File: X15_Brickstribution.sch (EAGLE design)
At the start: 85 parts, among them Q1 310mA/60V/1.6Ω, U5 IC_L4970A, U6 DIODE_STPS1545CT, U7 IC_L4970A, U8 DIODE_STPS1545CT

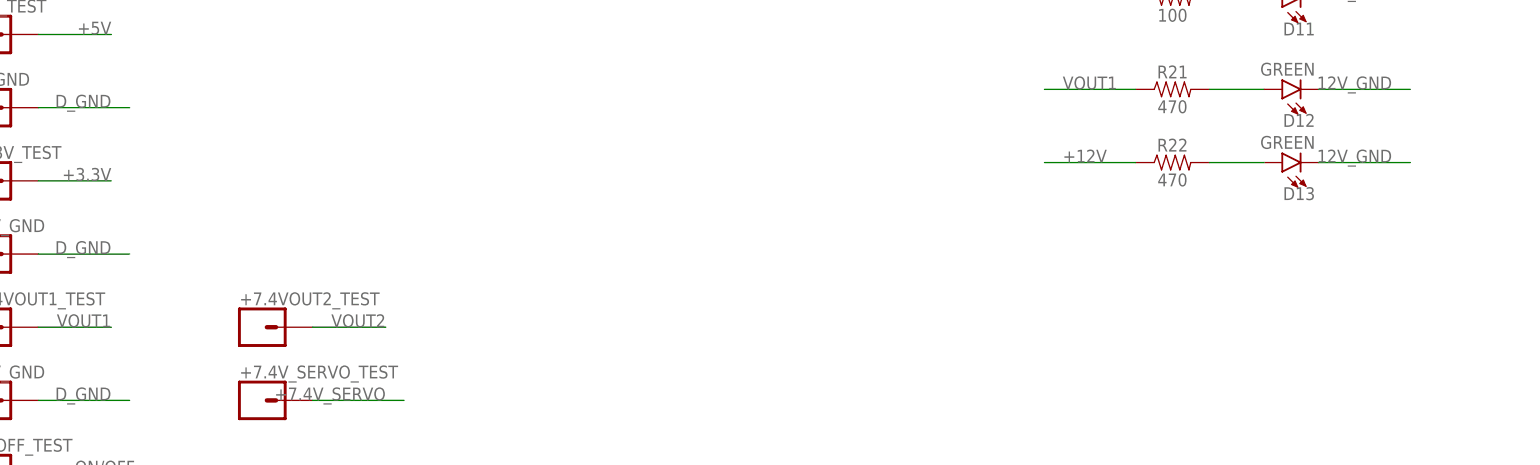
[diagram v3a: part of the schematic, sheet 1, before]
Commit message: Revision V3 Schematic - LED's added for current source
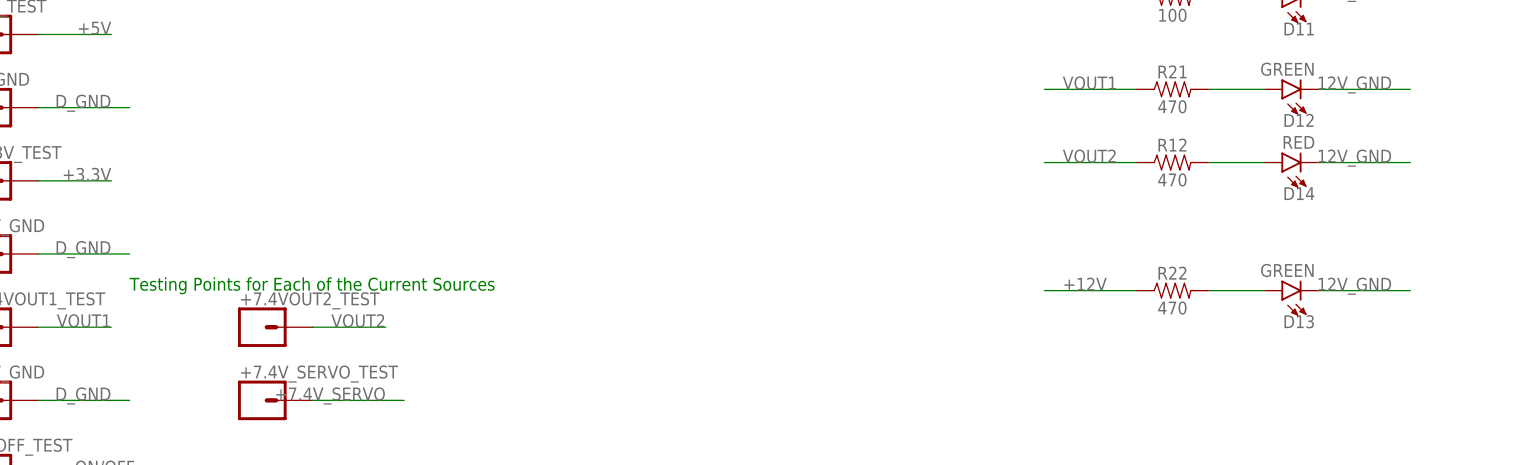
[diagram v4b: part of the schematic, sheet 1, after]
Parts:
- added D14: RED, SparkFun-LED:LED-RED0603
- added R12: 470, SparkFun-Resistors:470OHM-0603-1/10W-1%
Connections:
- new net N$11: D14.A, R12.2
- net 12V_GND: now also D14.C
- net VOUT2: now also R12.1
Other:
- note added: "Testing Points for Each of the Current Sources"
- moved on the sheet: D13, R22
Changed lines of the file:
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@@
 <part name="BACKPLANE_POWER" library="X15_Brickstribution" deviceset="CONN_MPPT-10-01-01-L-RA-SD" device=""/>
 <part name="U$2" library="X15_Brickstribution" deviceset="CONN_BMR480_CONNECTOR" device=""/>
+<part name="R12" library="SparkFun-Resistors" library_urn="urn:adsk.eagle:library:532" deviceset="470OHM" device="-0603-1/10W-1%" package3d_urn="urn:adsk.eagle:package:39650/1" value="470"/>
+<part name="D14" library="SparkFun-LED" library_urn="urn:adsk.eagle:library:529" deviceset="LED-RED" device="0603" package3d_urn="urn:adsk.eagle:package:39354/1" value="RED"/>
 </parts>
 <sheets>
@@
 <text x="227.838" y="124.206" size="1.4224" layer="91">Latch that keeps ON/OFF low after it first goes low</text>
 <text x="317.754" y="125.73" size="2.1844" layer="91">LED Testing</text>
+<text x="170.18" y="35.56" size="1.778" layer="91">Testing Points for Each of the Current Sources</text>
 </plain>
 <instances>
@@
 <attribute name="VALUE" x="334.772" y="65.405" size="1.778" layer="96" font="vector" rot="R180" align="top-left"/>
 </instance>
-<instance part="R22" gate="G$1" x="314.96" y="53.34" smashed="yes">
-<attribute name="NAME" x="314.96" y="54.864" size="1.778" layer="95" font="vector" align="bottom-center"/>
-<attribute name="VALUE" x="314.96" y="51.816" size="1.778" layer="96" font="vector" align="top-center"/>
-</instance>
-<instance part="D13" gate="G$1" x="330.2" y="53.34" smashed="yes" rot="R90">
-<attribute name="NAME" x="334.772" y="49.911" size="1.778" layer="95" font="vector" rot="R180"/>
-<attribute name="VALUE" x="334.772" y="55.245" size="1.778" layer="96" font="vector" rot="R180" align="top-left"/>
+<instance part="R22" gate="G$1" x="314.96" y="35.56" smashed="yes">
+<attribute name="NAME" x="314.96" y="37.084" size="1.778" layer="95" font="vector" align="bottom-center"/>
+<attribute name="VALUE" x="314.96" y="34.036" size="1.778" layer="96" font="vector" align="top-center"/>
+</instance>
+<instance part="D13" gate="G$1" x="330.2" y="35.56" smashed="yes" rot="R90">
+<attribute name="NAME" x="334.772" y="32.131" size="1.778" layer="95" font="vector" rot="R180"/>
+<attribute name="VALUE" x="334.772" y="37.465" size="1.778" layer="96" font="vector" rot="R180" align="top-left"/>
 </instance>
 <instance part="BACKPLANE_POWER" gate="A" x="355.6" y="180.34" smashed="yes">
@@
 </instance>
 <instance part="U$2" gate="G$1" x="53.34" y="198.12" smashed="yes"/>
+<instance part="R12" gate="G$1" x="314.96" y="53.34" smashed="yes">
+<attribute name="NAME" x="314.96" y="54.864" size="1.778" layer="95" font="vector" align="bottom-center"/>
+<attribute name="VALUE" x="314.96" y="51.816" size="1.778" layer="96" font="vector" align="top-center"/>
+</instance>
+<instance part="D14" gate="G$1" x="330.2" y="53.34" smashed="yes" rot="R90">
+<attribute name="NAME" x="334.772" y="49.911" size="1.778" layer="95" font="vector" rot="R180"/>
+<attribute name="VALUE" x="334.772" y="55.245" size="1.778" layer="96" font="vector" rot="R180" align="top-left"/>
+</instance>
 </instances>
 <busses>
@@
 <segment>
 <pinref part="D13" gate="G$1" pin="C"/>
+<wire x1="335.28" y1="35.56" x2="347.98" y2="35.56" width="0.1524" layer="91"/>
+<label x="345.44" y="35.56" size="1.778" layer="95" align="bottom-right"/>
+</segment>
+<segment>
 <wire x1="335.28" y1="53.34" x2="347.98" y2="53.34" width="0.1524" layer="91"/>
 <label x="345.44" y="53.34" size="1.778" layer="95" align="bottom-right"/>
+<pinref part="D14" gate="G$1" pin="C"/>
 </segment>
 </net>
@@
 <segment>
 <pinref part="R22" gate="G$1" pin="1"/>
-<wire x1="309.88" y1="53.34" x2="297.18" y2="53.34" width="0.1524" layer="91"/>
-<label x="299.72" y="53.34" size="1.778" layer="95"/>
+<wire x1="309.88" y1="35.56" x2="297.18" y2="35.56" width="0.1524" layer="91"/>
+<label x="299.72" y="35.56" size="1.778" layer="95"/>
 </segment>
 </net>
@@
 <label x="205.74" y="30.48" size="1.778" layer="95" align="bottom-right"/>
 </segment>
+<segment>
+<pinref part="R12" gate="G$1" pin="1"/>
+<wire x1="309.88" y1="53.34" x2="297.18" y2="53.34" width="0.1524" layer="91"/>
+<label x="299.72" y="53.34" size="1.778" layer="95"/>
+</segment>
 </net>
 <net name="VOUT1" class="0">
@@
 <pinref part="R22" gate="G$1" pin="2"/>
 <pinref part="D13" gate="G$1" pin="A"/>
-<wire x1="320.04" y1="53.34" x2="327.66" y2="53.34" width="0.1524" layer="91"/>
+<wire x1="320.04" y1="35.56" x2="327.66" y2="35.56" width="0.1524" layer="91"/>
 </segment>
 </net>
@@
 </segment>
 </net>
+<net name="N$11" class="0">
+<segment>
+<pinref part="R12" gate="G$1" pin="2"/>
+<wire x1="320.04" y1="53.34" x2="327.66" y2="53.34" width="0.1524" layer="91"/>
+<pinref part="D14" gate="G$1" pin="A"/>
+</segment>
+</net>

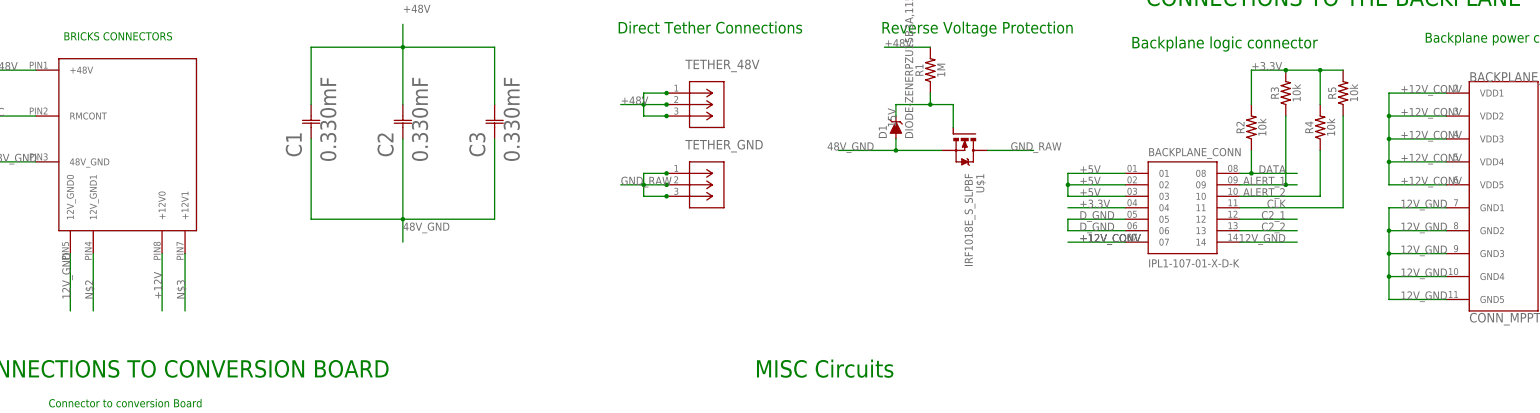
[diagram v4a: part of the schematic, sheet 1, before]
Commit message: 48V Components Added to PCB
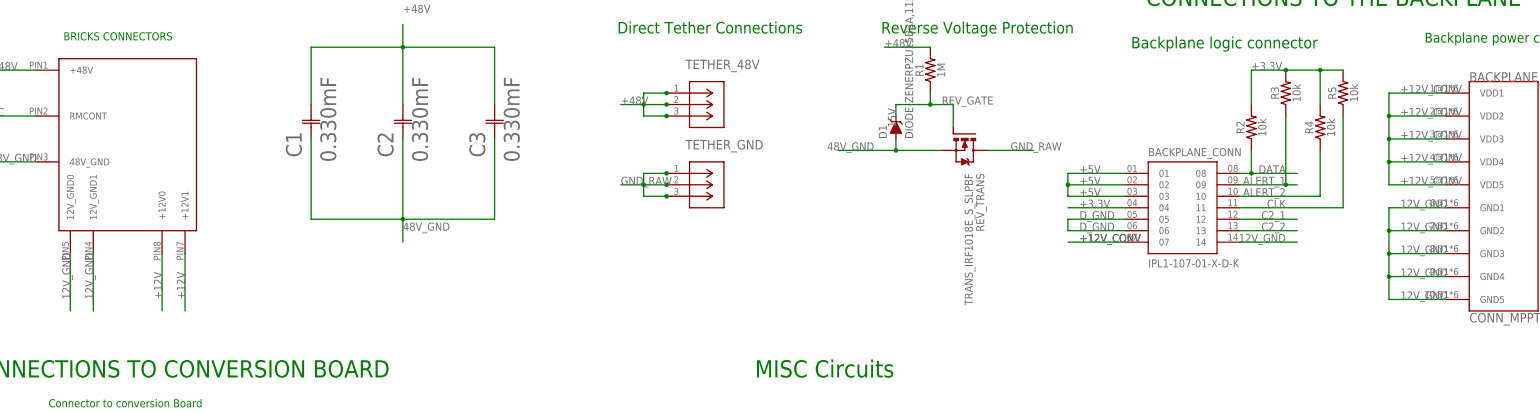
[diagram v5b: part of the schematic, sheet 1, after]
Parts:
- removed U$1: IRF1018E_S_SLPBF, X15_Brickstribution:IRF1018E_S_SLPBF
- added REV_TRANS: TRANS_IRF1018E_S_SLPBF, X15_Brickstribution:TRANS_IRF1018E_S_SLPBF
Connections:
- removed net N$1: D1.C, R1.1, U$1.G
- removed net N$2: U$2.12V_GND1
- removed net N$3: U$2.+12V1
- new net REV_GATE: D1.C, R1.1, REV_TRANS.G
- net +12V: now also U$2.+12V1
- net 12V_GND: now also U$2.12V_GND1
- net 48V_GND: now also REV_TRANS.S; no longer U$1.S
- net GND_RAW: now also REV_TRANS.D; no longer U$1.D
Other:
- moved on the sheet: BACKPLANE_POWER, U$7
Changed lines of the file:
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@@
 <parts>
 <part name="FRAME1" library="frames" library_urn="urn:adsk.eagle:library:229" deviceset="A3L-LOC" device=""/>
-<part name="U$1" library="X15_Brickstribution" deviceset="IRF1018E_S_SLPBF" device=""/>
 <part name="R1" library="SparkFun-Resistors" library_urn="urn:adsk.eagle:library:532" deviceset="1MOHM" device="-0603-1/4W-5%" package3d_urn="urn:adsk.eagle:package:39650/1" value="1M"/>
 <part name="D1" library="SparkFun-DiscreteSemi" deviceset="DIODE-ZENER" device="PZU15B3A,115" package3d_urn="urn:adsk.eagle:package:38441/1"/>
@@
 <part name="R12" library="SparkFun-Resistors" library_urn="urn:adsk.eagle:library:532" deviceset="470OHM" device="-0603-1/10W-1%" package3d_urn="urn:adsk.eagle:package:39650/1" value="470"/>
 <part name="D14" library="SparkFun-LED" library_urn="urn:adsk.eagle:library:529" deviceset="LED-RED" device="0603" package3d_urn="urn:adsk.eagle:package:39354/1" value="RED"/>
+<part name="REV_TRANS" library="X15_Brickstribution" deviceset="TRANS_IRF1018E_S_SLPBF" device=""/>
 </parts>
 <sheets>
@@
 <attribute name="SHEET" x="357.505" y="5.08" size="2.54" layer="94"/>
 </instance>
-<instance part="U$1" gate="G$1" x="236.22" y="190.5" smashed="yes" rot="R270">
-<attribute name="NAME" x="238.760440625" y="185.41866875" size="1.778309375" layer="95" rot="R270"/>
-<attribute name="VALUE" x="236.22" y="185.41125" size="1.780040625" layer="96" rot="R270"/>
-</instance>
 <instance part="R1" gate="G$1" x="228.6" y="208.28" smashed="yes" rot="R90">
 <attribute name="NAME" x="227.076" y="208.28" size="1.778" layer="95" font="vector" rot="R90" align="bottom-center"/>
@@
 <attribute name="NAME" x="334.772" y="49.911" size="1.778" layer="95" font="vector" rot="R180"/>
 <attribute name="VALUE" x="334.772" y="55.245" size="1.778" layer="96" font="vector" rot="R180" align="top-left"/>
+</instance>
+<instance part="REV_TRANS" gate="G$1" x="236.22" y="190.5" smashed="yes" rot="R270">
+<attribute name="NAME" x="238.760440625" y="185.41866875" size="1.778309375" layer="95" rot="R270"/>
+<attribute name="VALUE" x="236.22" y="185.41125" size="1.780040625" layer="96" rot="R270"/>
 </instance>
 </instances>
@@
 </segment>
 <segment>
-<pinref part="U$1" gate="G$1" pin="S"/>
 <wire x1="220.98" y1="193.04" x2="220.98" y2="190.5" width="0.1524" layer="91"/>
 <wire x1="220.98" y1="190.5" x2="231.14" y2="190.5" width="0.1524" layer="91"/>
@@
 <label x="205.74" y="190.5" size="1.778" layer="95"/>
 <pinref part="D1" gate="G$1" pin="A"/>
+<pinref part="REV_TRANS" gate="G$1" pin="S"/>
 </segment>
 <segment>
@@
 <pinref part="D14" gate="G$1" pin="C"/>
 </segment>
+<segment>
+<wire x1="43.18" y1="167.64" x2="43.18" y2="154.94" width="0.1524" layer="91"/>
+<label x="43.18" y="157.48" size="1.778" layer="95" rot="R90"/>
+<pinref part="U$2" gate="G$1" pin="12V_GND1"/>
+</segment>
 </net>
 <net name="+12V" class="0">
@@
 <label x="299.72" y="35.56" size="1.778" layer="95"/>
 </segment>
-</net>
-<net name="N$1" class="0">
+<segment>
+<wire x1="63.5" y1="167.64" x2="63.5" y2="154.94" width="0.1524" layer="91"/>
+<label x="63.5" y="157.48" size="1.778" layer="95" rot="R90"/>
+<pinref part="U$2" gate="G$1" pin="+12V1"/>
+</segment>
+</net>
+<net name="REV_GATE" class="0">
 <segment>
 <wire x1="220.98" y1="198.12" x2="220.98" y2="200.66" width="0.1524" layer="91"/>
-<pinref part="U$1" gate="G$1" pin="G"/>
 <wire x1="220.98" y1="200.66" x2="228.6" y2="200.66" width="0.1524" layer="91"/>
 <wire x1="228.6" y1="200.66" x2="233.68" y2="200.66" width="0.1524" layer="91"/>
@@
 <junction x="228.6" y="200.66"/>
 <pinref part="D1" gate="G$1" pin="C"/>
+<label x="231.14" y="200.66" size="1.778" layer="95"/>
+<pinref part="REV_TRANS" gate="G$1" pin="G"/>
 </segment>
 </net>
 <net name="GND_RAW" class="0">
 <segment>
-<pinref part="U$1" gate="G$1" pin="D"/>
 <wire x1="241.3" y1="190.5" x2="251.46" y2="190.5" width="0.1524" layer="91"/>
 <label x="246.38" y="190.5" size="1.778" layer="95"/>
+<pinref part="REV_TRANS" gate="G$1" pin="D"/>
 </segment>
 <segment>
@@
 </segment>
 </net>
-<net name="N$2" class="0">
-<segment>
-<wire x1="43.18" y1="167.64" x2="43.18" y2="154.94" width="0.1524" layer="91"/>
-<label x="43.18" y="157.48" size="1.778" layer="95" rot="R90"/>
-<pinref part="U$2" gate="G$1" pin="12V_GND1"/>
-</segment>
-</net>
-<net name="N$3" class="0">
-<segment>
-<wire x1="63.5" y1="167.64" x2="63.5" y2="154.94" width="0.1524" layer="91"/>
-<label x="63.5" y="157.48" size="1.778" layer="95" rot="R90"/>
-<pinref part="U$2" gate="G$1" pin="+12V1"/>
-</segment>
-</net>

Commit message: Board & Schematic Review Iteration
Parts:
- removed CONV_CONN: TSW-110-07-G-S, X15_Brickstribution:TSW-110-07-G-S
- removed R2, R3, R4, R5: 10k, SparkFun-Resistors:10KOHM-0603-1/10W-1%
- removed U$7: CONN_MPPT-10-01-01-L-RA-SD, X15_Brickstribution:CONN_MPPT-10-01-01-L-RA-SD
- added H1, H2, H3, H4: 6-32-HOLE, X15_Brickstribution:6-32-HOLE
- added J1: IPL1-104-01-X-S-K, X15_Brickstribution:IPL1-104-01-X-S-K
- added U$1: CONN_DISTRIBUTION_TO_CONVERSION, X15_Brickstribution:CONN_DISTRIBUTION_TO_CONVERSION
- R31: value DIODE_RBQ30NS45AFHTLTRANS_R5009FNJ_ROM-M -> DIODE_RBQ30NS45AFHTL; device X15_Brickstribution:DIODE_RBQ30NS45AFHTLTRANS_R5009FNJ_ROM-M -> X15_Brickstribution:DIODE_RBQ30NS45AFHTL
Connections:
- removed net ALERT_1: BACKPLANE_CONN.09, R3.1
- removed net ALERT_2: BACKPLANE_CONN.10, R4.1
- removed net C2_1: BACKPLANE_CONN.12
- removed net C2_2: BACKPLANE_CONN.13
- removed net CLK: BACKPLANE_CONN.11, R5.1
- removed net DATA: BACKPLANE_CONN.08, R2.1
- removed net D_GND: 3.3V_GND.1, 5V_GND.1, 7.4V_GND.1, BACKPLANE_CONN.05, BACKPLANE_CONN.06, CONV_CONN.10, CONV_CONN.9, D10.C, D11.C
- removed net NC: U$2.RMCONT, U5.RST_DLY, U5.RST_OUT, U5.SYNC, U7.RST_DLY, U7.RST_OUT, U7.SYNC
- net +12V: no longer +12V_TEST.1, R9.1
- net +12V_CONV: now also +12V_TEST.1, R9.1, U$1.VIN+; no longer CONV_CONN.1, CONV_CONN.2
- net +3.3V: now also U$1.VOUT+_3; no longer CONV_CONN.7, CONV_CONN.8, R2.2, R3.2, R4.2, R5.2
- net +5V: now also U$1.VOUT+_5; no longer CONV_CONN.5, CONV_CONN.6
- net +7.4V_SERVO: now also J1.01, J1.02; no longer U$7.VDD1, U$7.VDD2, U$7.VDD3, U$7.VDD4, U$7.VDD5
- net 12V_GND: now also 3.3V_GND.1, 5V_GND.1, 7.4V_GND.1, BACKPLANE_CONN.05, BACKPLANE_CONN.06, D10.C, D11.C, J1.03, J1.04, U$1.VIN-, U$1.VOUT-; no longer CONV_CONN.3, CONV_CONN.4, U$7.GND1, U$7.GND2, U$7.GND3, U$7.GND4, U$7.GND5
